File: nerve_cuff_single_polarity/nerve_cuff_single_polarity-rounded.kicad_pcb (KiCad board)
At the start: 2 copper layers, 3.8 x 5.1 mm, 0 parts

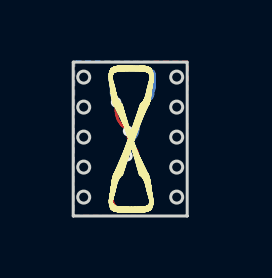
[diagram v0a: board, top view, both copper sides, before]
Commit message: fixing minor DRC problems for z cuff
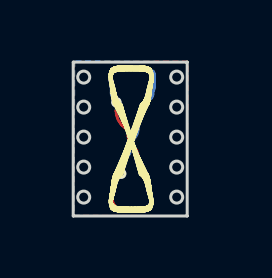
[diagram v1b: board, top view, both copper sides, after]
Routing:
- net (no net): track 12.6 -> 11.7 mm, vias 3 -> 2

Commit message: adding pads to single polarity cuff
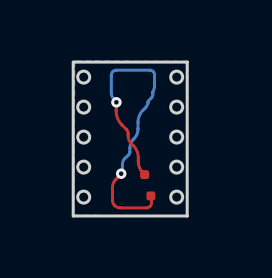
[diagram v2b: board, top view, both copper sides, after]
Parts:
- added REF**: small_pad_nerve_cuff, nerve_cuff_pads:small_pad_nerve_cuff, F.Cu at (93.9, 30.0)
- added REF**: small_pad_nerve_cuff, nerve_cuff_pads:small_pad_nerve_cuff, F.Cu at (93.7, 29.2)

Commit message: cleaning up XY gradient board, updating pads
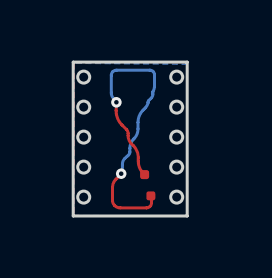
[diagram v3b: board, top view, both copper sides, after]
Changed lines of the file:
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@@
     (connect_pads (clearance 0.01))
     (min_thickness 0.1) (filled_areas_thickness no)
-    (fill (thermal_gap 0.01) (thermal_bridge_width 0.1) (island_removal_mode 1) (island_area_min 10))
+    (fill yes (thermal_gap 0.05) (thermal_bridge_width 0.1) (island_removal_mode 1) (island_area_min 10))
     (polygon
       (pts
-        (xy 91.32 25.49)
-        (xy 91.31 30.61)
-        (xy 95.09 30.62)
-        (xy 95.13 25.47)
-        (xy 91.33 25.49)
+        (xy 91.33 25.54)
+        (xy 91.32 30.63)
+        (xy 95.11 30.63)
+        (xy 95.1 25.5)
+        (xy 91.33 25.52)
+        (xy 91.33 25.6)
       )
     )
@@
     (connect_pads (clearance 0.01))
     (min_thickness 0.1) (filled_areas_thickness no)
-    (fill (thermal_gap 0.05) (thermal_bridge_width 0.1) (island_removal_mode 1) (island_area_min 10))
+    (fill yes (thermal_gap 0.05) (thermal_bridge_width 0.1) (island_removal_mode 1) (island_area_min 10))
     (polygon
       (pts
-        (xy 91.35 25.46)
+        (xy 91.33 25.54)
         (xy 91.32 30.61)
         (xy 95.09 30.64)
-        (xy 95.1 25.49)
-        (xy 91.36 25.46)
+        (xy 95.11 25.57)
+        (xy 91.37 25.54)
       )
     )

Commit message: updating constraints for single polarity board
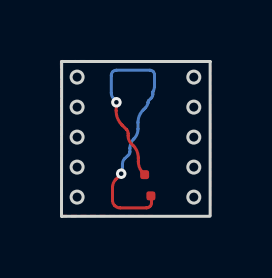
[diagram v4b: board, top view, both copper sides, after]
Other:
- board size 3.8 x 5.1 mm -> 5 x 5.2 mm
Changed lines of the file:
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@@
     (pad "1" smd roundrect (at 0 0) (size 0.3 0.3) (layers "F.Cu" "F.Paste" "F.Mask") (roundrect_rratio 0.25))
   )
-  (gr_circle (center 91.65 27) (end 91.85 27)
+  (gr_circle (center 91.43 27) (end 91.63 27)
     (stroke (width 0.1) (type default)) (fill none) (layer "Edge.Cuts"))
-  (gr_circle (center 91.65 29) (end 91.85 29)
+  (gr_circle (center 91.43 29) (end 91.63 29)
     (stroke (width 0.1) (type default)) (fill none) (layer "Edge.Cuts"))
-  (gr_circle (center 91.65 28) (end 91.85 28)
+  (gr_circle (center 91.43 28) (end 91.63 28)
     (stroke (width 0.1) (type default)) (fill none) (layer "Edge.Cuts"))
-  (gr_line (start 91.3 25.5) (end 91.3 30.63)
+  (gr_line (start 90.915 25.48) (end 90.91 30.635)
     (stroke (width 0.1) (type default)) (layer "Edge.Cuts"))
-  (gr_circle (center 94.75 26) (end 94.95 26)
+  (gr_circle (center 95.32 26) (end 95.52 26)
     (stroke (width 0.1) (type default)) (fill none) (layer "Edge.Cuts"))
-  (gr_circle (center 94.75 29) (end 94.95 29)
+  (gr_circle (center 95.32 29) (end 95.52 29)
     (stroke (width 0.1) (type default)) (fill none) (layer "Edge.Cuts"))
-  (gr_circle (center 94.75 28) (end 94.95 28)
+  (gr_circle (center 95.32 28) (end 95.52 28)
     (stroke (width 0.1) (type default)) (fill none) (layer "Edge.Cuts"))
-  (gr_circle (center 91.65 26) (end 91.85 26)
+  (gr_circle (center 91.43 26) (end 91.63 26)
     (stroke (width 0.1) (type default)) (fill none) (layer "Edge.Cuts"))
-  (gr_line (start 95.1 25.5) (end 95.1 30.63)
+  (gr_line (start 95.865 30.61) (end 95.865 25.48)
     (stroke (width 0.1) (type default)) (layer "Edge.Cuts"))
-  (gr_circle (center 94.75 30) (end 94.95 30)
+  (gr_circle (center 95.32 30) (end 95.52 30)
     (stroke (width 0.1) (type default)) (fill none) (layer "Edge.Cuts"))
-  (gr_line (start 91.3 25.5) (end 95.1 25.5)
+  (gr_line (start 90.915 25.48) (end 95.865 25.48)
     (stroke (width 0.1) (type default)) (layer "Edge.Cuts"))
-  (gr_circle (center 94.75 27) (end 94.95 27)
+  (gr_circle (center 95.32 27) (end 95.52 27)
     (stroke (width 0.1) (type default)) (fill none) (layer "Edge.Cuts"))
-  (gr_line (start 91.3 30.63) (end 95.1 30.63)
+  (gr_line (start 90.91 30.64) (end 95.86 30.64)
     (stroke (width 0.1) (type default)) (layer "Edge.Cuts"))
-  (gr_circle (center 91.65 30) (end 91.85 30)
+  (gr_circle (center 91.43 30) (end 91.63 30)
     (stroke (width 0.1) (type default)) (fill none) (layer "Edge.Cuts"))
   (dimension (type aligned) (layer "F.SilkS")
-    (pts (xy 95.13 25.47) (xy 95.1 30.63))
-    (height -6.782918)
-    (gr_text "5.1601 mm" (at 100.747822 28.082749 89.66688876) (layer "F.SilkS")
+    (pts (xy 90.91 25.51) (xy 95.86 25.51))
+    (height -1.78)
+    (gr_text "4.9500 mm" (at 93.385 22.58) (layer "F.SilkS")
       (effects (font (size 1 1) (thickness 0.15)))
     )
@@
   )
   (dimension (type aligned) (layer "F.SilkS")
-    (pts (xy 91.3 25.5) (xy 95.1 25.49))
-    (height -2.366984)
-    (gr_text "3.8000 mm" (at 93.190745 21.978028 0.1507780191) (layer "F.SilkS")
+    (pts (xy 95.603517 30.611984) (xy 91.713517 30.551984))
+    (height -4.118506)
+    (gr_text "3.8905 mm" (at 93.612736 33.550137 -0.8836694578) (layer "F.SilkS")
       (effects (font (size 1 1) (thickness 0.15)))
     )
@@
     (connect_pads (clearance 0.01))
     (min_thickness 0.1) (filled_areas_thickness no)
-    (fill yes (thermal_gap 0.05) (thermal_bridge_width 0.1) (island_removal_mode 1) (island_area_min 10))
+    (fill yes (thermal_gap 0.1) (thermal_bridge_width 0.1) (island_removal_mode 1) (island_area_min 10))
     (polygon
       (pts
-        (xy 91.33 25.54)
-        (xy 91.32 30.63)
-        (xy 95.11 30.63)
-        (xy 95.1 25.5)
-        (xy 91.33 25.52)
-        (xy 91.33 25.6)
+        (xy 95.27 25.48)
+        (xy 90.88 25.45)
+        (xy 90.9 30.61)
+        (xy 95.88 30.62)
+        (xy 95.88 25.49)
       )
     )
@@
     (polygon
       (pts
-        (xy 91.33 25.54)
-        (xy 91.32 30.61)
-        (xy 95.09 30.64)
-        (xy 95.11 25.57)
-        (xy 91.37 25.54)
+        (xy 90.88 25.52)
+        (xy 90.9 30.66)
+        (xy 95.87 30.62)
+        (xy 95.87 25.46)
+        (xy 91.35 25.45)
       )
     )
